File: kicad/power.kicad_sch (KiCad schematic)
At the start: 37 parts, among them U1 MIMXRT1171DVMAB, U4 TPS62086, U5 TPS62825, Y1 24MHz, Y2 32.768kHz

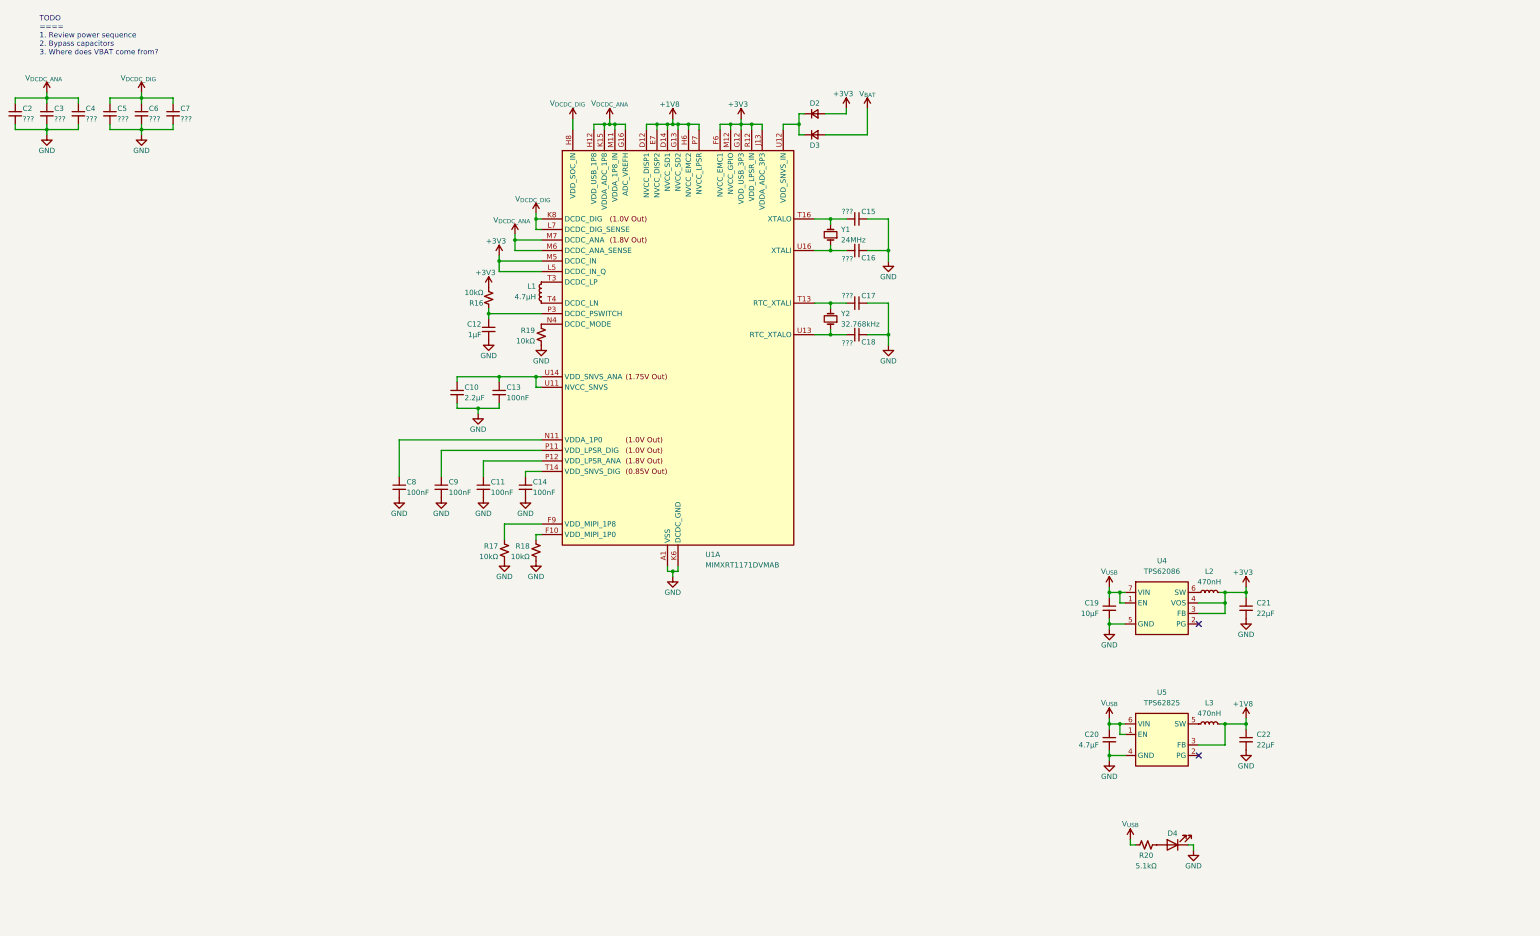
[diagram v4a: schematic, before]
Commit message: added magnetometer to schematic
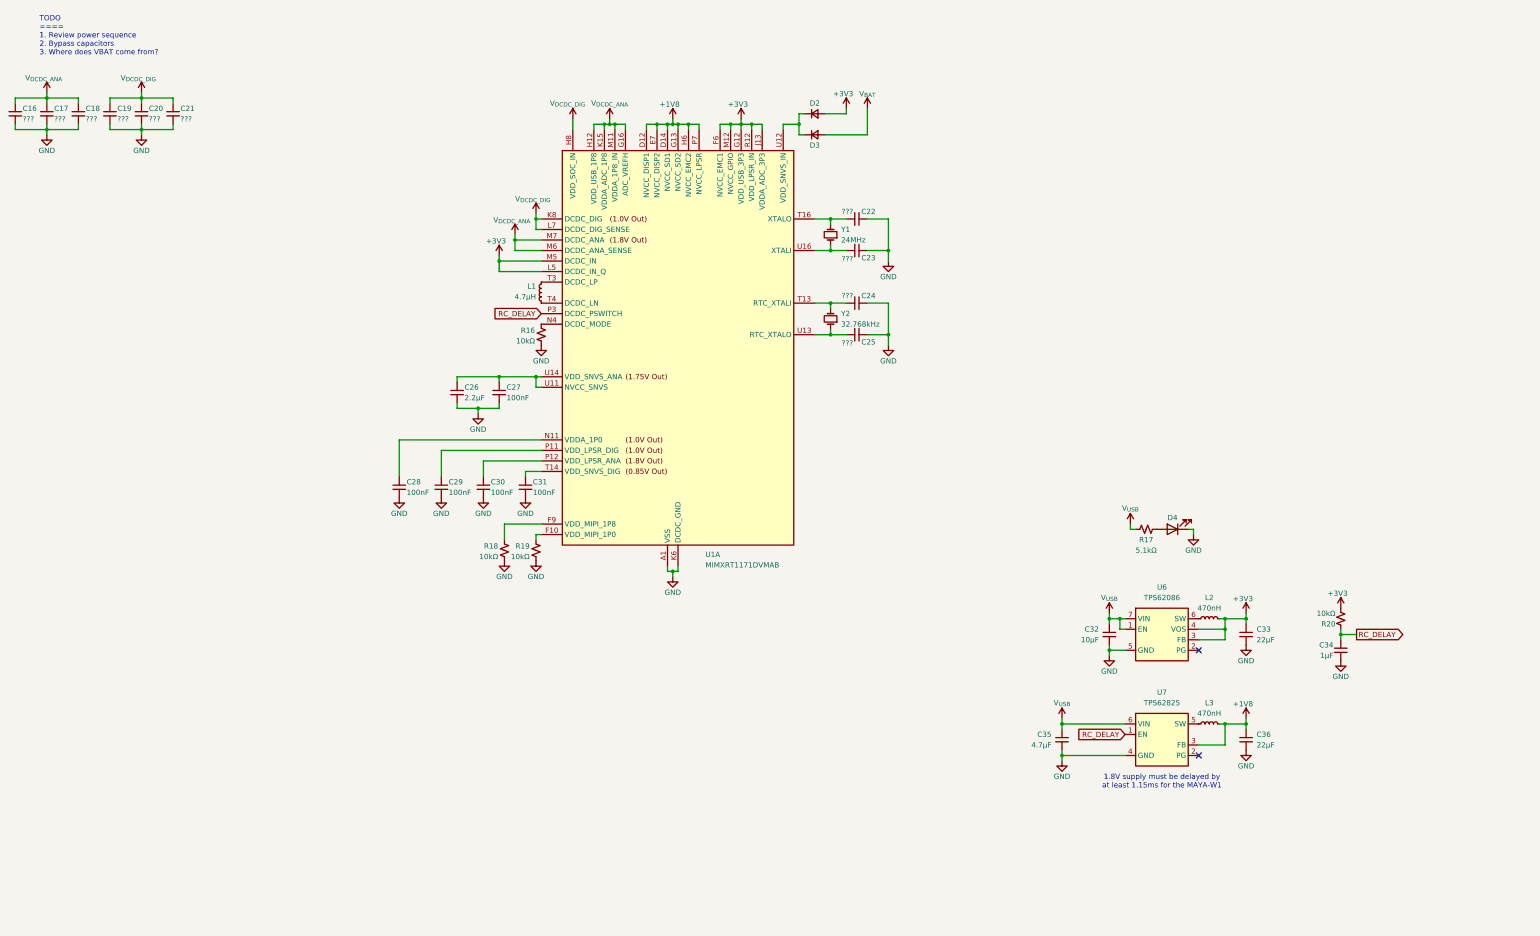
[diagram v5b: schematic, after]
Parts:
- removed C12: 1μF, symbol Device:C_Small
- removed R16: 10kΩ, symbol Device:R_Small_US
- added C34: 1μF, symbol Device:C_Small
- added R20: 10kΩ, symbol Device:R_Small_US
- renumbered C2 to C16, C3 to C17, C4 to C18, C5 to C19, C6 to C20, C7 to C21, C15 to C22, C16 to C23, C17 to C24, C18 to C25, C10 to C26, C13 to C27, C8 to C28, C9 to C29, C11 to C30, C14 to C31, C19 to C32, C21 to C33, C20 to C35, C22 to C36, R19 to R16, R20 to R17, R17 to R18, R18 to R19, U4 to U6, U5 to U7
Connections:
- net +3V3: now also R20.2
- net GND: now also C34.2
- net V_{USB}: no longer U7.1 (EN)
- net RC_DELAY: now reaches U1.P3 (DCDC_PSWITCH)
- net RC_DELAY: now also U7.1 (EN), C34.1, R20.1
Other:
- note added: "1.8V supply must be delayed by at least 1.15ms for the MAYA-W1"
- moved on the sheet: C32, C33, C35, D4, L2, R17, U6

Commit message: added bypass caps
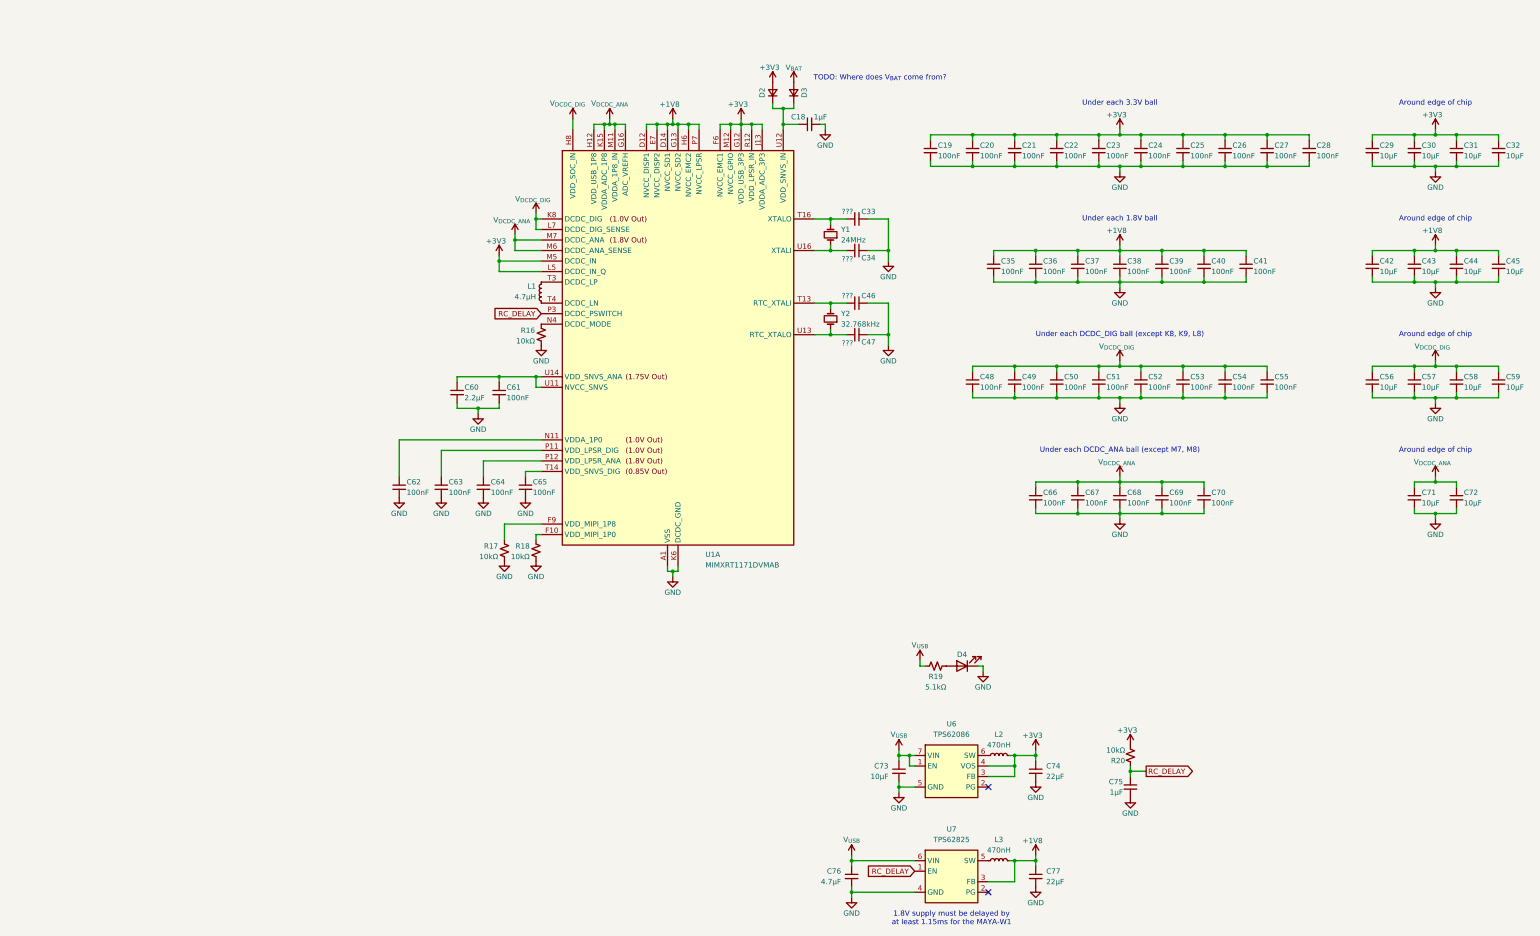
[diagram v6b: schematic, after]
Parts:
- removed C16, C17: ???, symbol Device:C_Small
- added C22, C23, C24, C25, C26, C27, C28, C35, C36, C37, C38, C39, C40, C41, C48, C49, C50, C51, C52, C53, C54, C55, C66, C67, C68, C69, C70: 100nF, symbol Device:C_Small
- added C29, C30, C31, C32, C42, C43, C44, C45, C56, C57, C58, C59, C71, C72: 10μF, symbol Device:C_Small
- C18: value ??? -> 1μF
- C19, C20, C21: value ??? -> 100nF
- renumbered C22 to C33, C23 to C34, C24 to C46, C25 to C47, C26 to C60, C27 to C61, C28 to C62, C29 to C63, C30 to C64, C31 to C65, C32 to C73, C33 to C74, C34 to C75, C35 to C76, C36 to C77, R18 to R17, R19 to R18, R17 to R19
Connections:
- net +1V8: now also C35.1, C36.1, C37.1, C38.1, C39.1, C40.1, C41.1, C42.1, C43.1, C44.1, C45.1
- net +3V3: now also C19.1, C20.1, C21.1, C22.1, C23.1, C24.1, C25.1, C26.1, C27.1, C28.1, C29.1, C30.1, C31.1, C32.1
- net GND: now also C22.2, C23.2, C24.2, C25.2, C26.2, C27.2, C28.2, C29.2, C30.2, C31.2, C32.2, C35.2, C36.2, C37.2, C38.2, C39.2, C40.2, C41.2, C42.2, C43.2, C44.2, C45.2, C48.2, C49.2, C50.2, C51.2, C52.2, C53.2, C54.2, C55.2, C56.2, C57.2, C58.2, C59.2, C66.2, C67.2, C68.2, C69.2, C70.2, C71.2, C72.2
- net V_{DCDC_ANA}: now also C66.1, C67.1, C68.1, C69.1, C70.1, C71.1, C72.1; no longer C18.1
- net V_{DCDC_DIG}: now also C48.1, C49.1, C50.1, C51.1, C52.1, C53.1, C54.1, C55.1, C56.1, C57.1, C58.1, C59.1; no longer C19.1, C20.1, C21.1
- net at D2.1 (K), D3.1 (K), U1.U12 (VDD_SNVS_IN): now also C18.1
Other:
- note added: "Around edge of chip"
- note added: "TODO: Where does V_{BAT} come from?"
- note added: "Under each 1.8V ball"
- note added: "Under each 3.3V ball"
- note added: "Under each DCDC_ANA ball (except M7, M8)"
- note added: "Under each DCDC_DIG ball (except K8, K9, L8)"
- note removed: "TODO ==== 1. Review power sequence 2. Bypass capacitors 3. Where does VBAT come from?"
- moved on the sheet: C73, C74, C75, C76, C77, D4, L2, L3, R19, R20, U6, U7

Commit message: added KL26 (DAPLink HIC) to schematic
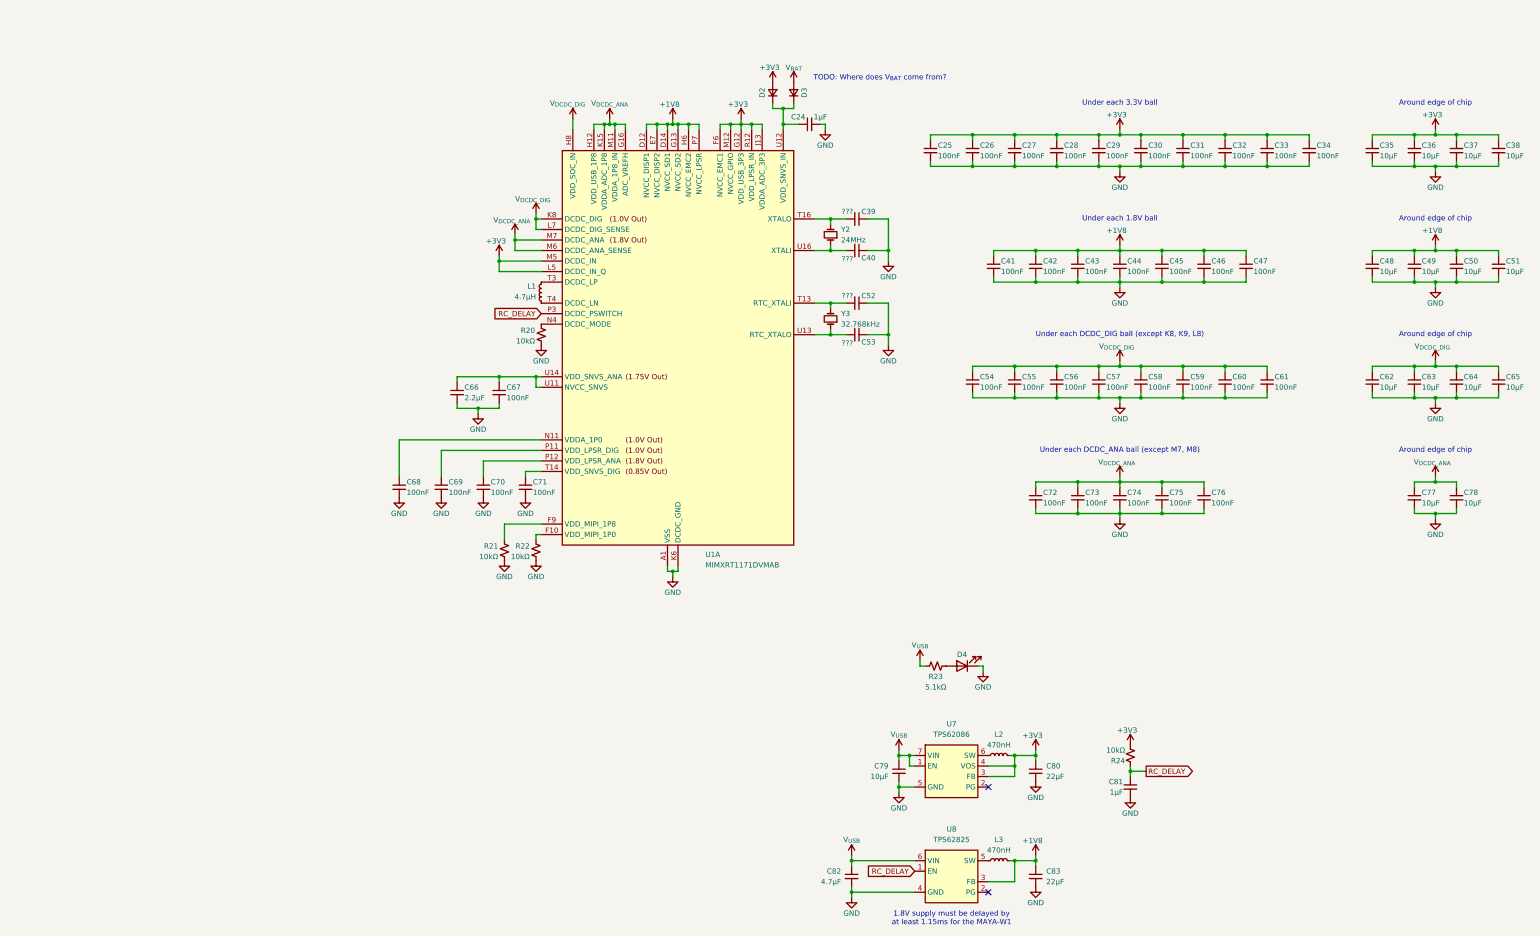
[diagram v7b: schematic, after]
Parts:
- renumbered C18 to C24, C19 to C25, C20 to C26, C21 to C27, C22 to C28, C23 to C29, C24 to C30, C25 to C31, C26 to C32, C27 to C33, C28 to C34, C29 to C35, C30 to C36, C31 to C37, C32 to C38, C33 to C39, C34 to C40, C35 to C41, C36 to C42, C37 to C43, C38 to C44, C39 to C45, C40 to C46, C41 to C47, C42 to C48, C43 to C49, C44 to C50, C45 to C51, C46 to C52, C47 to C53, C48 to C54, C49 to C55, C50 to C56, C51 to C57, C52 to C58, C53 to C59, C54 to C60, C55 to C61, C56 to C62, C57 to C63, C58 to C64, C59 to C65, C60 to C66, C61 to C67, C62 to C68, C63 to C69, C64 to C70, C65 to C71, C66 to C72, C67 to C73, C68 to C74, C69 to C75, C70 to C76, C71 to C77, C72 to C78, C73 to C79, C74 to C80, C75 to C81, C76 to C82, C77 to C83, R16 to R20, R17 to R21, R18 to R22, R19 to R23, R20 to R24, U6 to U7, U7 to U8, Y1 to Y2, Y2 to Y3

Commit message: added RTMC-G2-4IQ48 to schematic
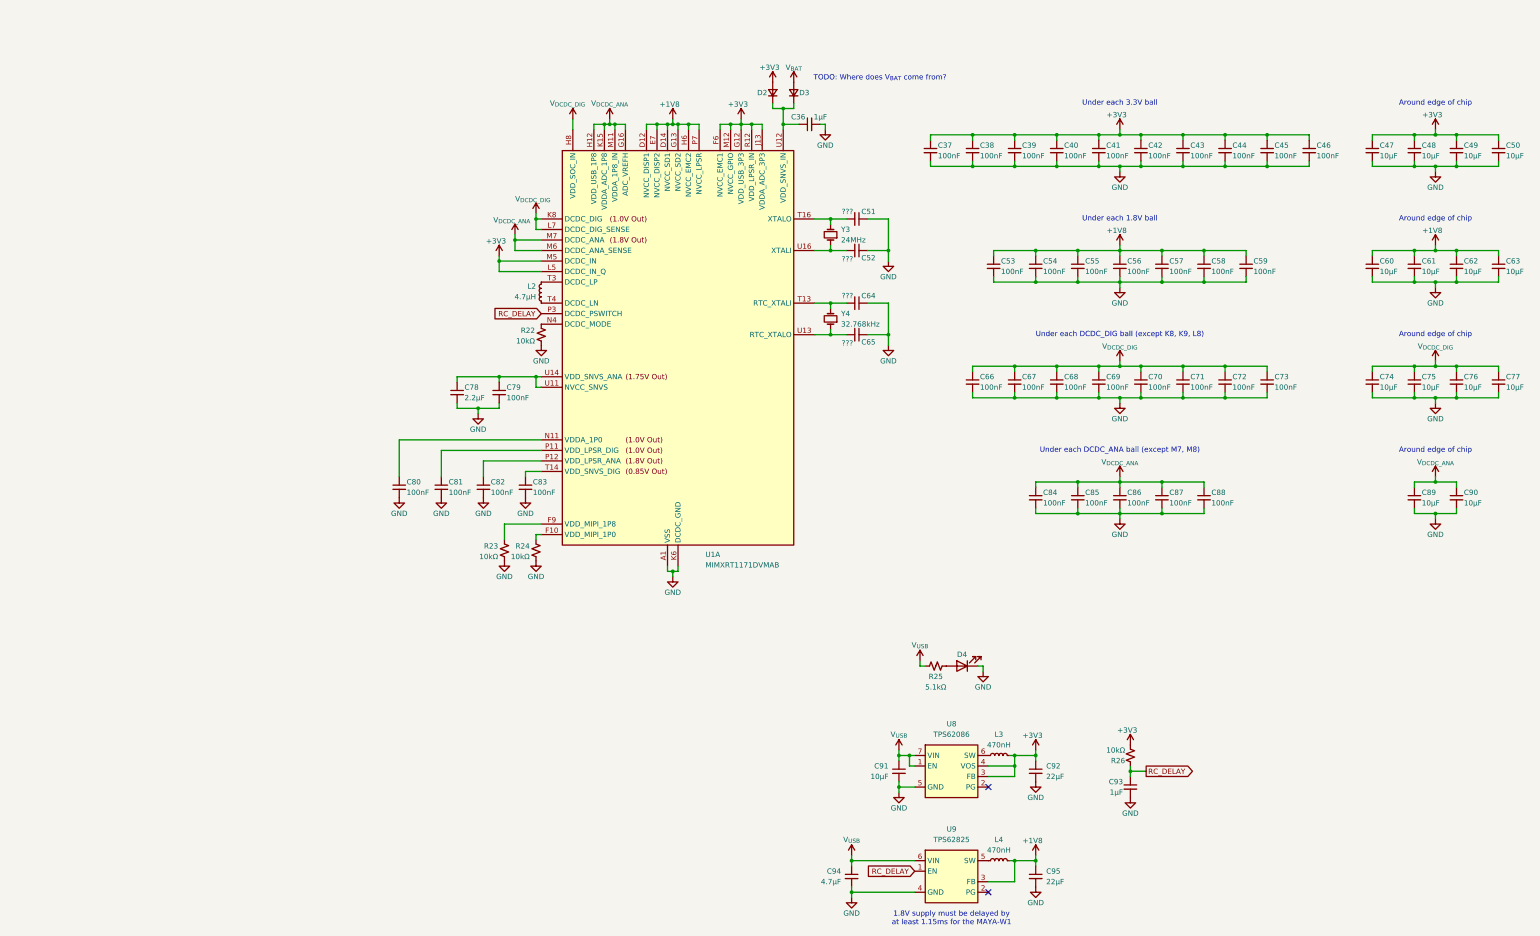
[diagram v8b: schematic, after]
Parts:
- renumbered C24 to C36, C25 to C37, C26 to C38, C27 to C39, C28 to C40, C29 to C41, C30 to C42, C31 to C43, C32 to C44, C33 to C45, C34 to C46, C35 to C47, C36 to C48, C37 to C49, C38 to C50, C39 to C51, C40 to C52, C41 to C53, C42 to C54, C43 to C55, C44 to C56, C45 to C57, C46 to C58, C47 to C59, C48 to C60, C49 to C61, C50 to C62, C51 to C63, C52 to C64, C53 to C65, C54 to C66, C55 to C67, C56 to C68, C57 to C69, C58 to C70, C59 to C71, C60 to C72, C61 to C73, C62 to C74, C63 to C75, C64 to C76, C65 to C77, C66 to C78, C67 to C79, C68 to C80, C69 to C81, C70 to C82, C71 to C83, C72 to C84, C73 to C85, C74 to C86, C75 to C87, C76 to C88, C77 to C89, C78 to C90, C79 to C91, C80 to C92, C81 to C93, C82 to C94, C83 to C95, L1 to L2, L2 to L3, L3 to L4, R20 to R22, R21 to R23, R22 to R24, R23 to R25, R24 to R26, U7 to U8, U8 to U9, Y2 to Y3, Y3 to Y4
